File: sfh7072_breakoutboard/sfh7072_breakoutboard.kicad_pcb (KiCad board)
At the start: 2 copper layers, 24.5 x 25 mm, 11 parts, among them J1 C_01x06, J2 C_01x04

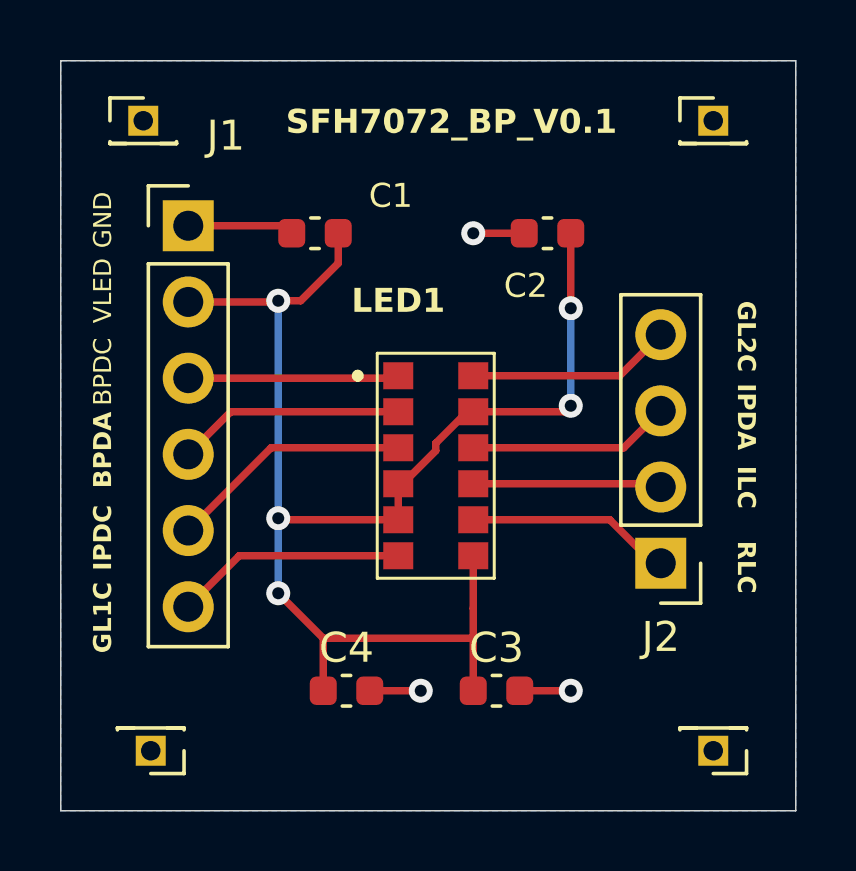
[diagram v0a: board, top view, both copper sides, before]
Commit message: sfh7072 board with separate anode for all leds
- separate anode and cathode connector for all leds
  and photodiodes

Signed-off-by: Mika Laitio <lamikr@gmail.com>
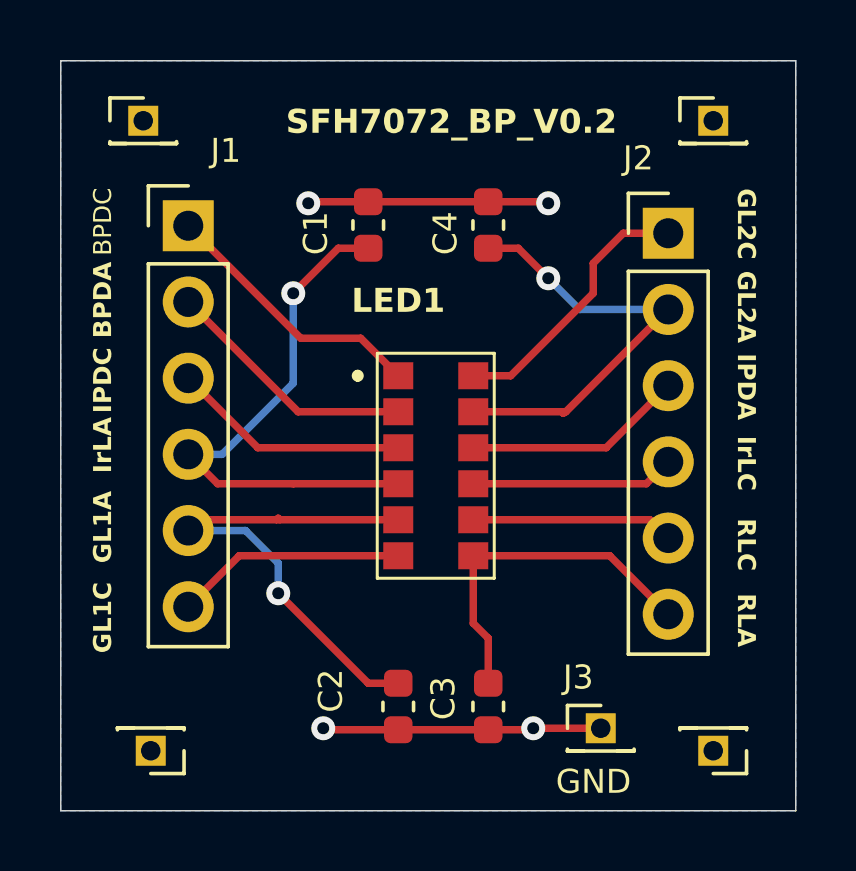
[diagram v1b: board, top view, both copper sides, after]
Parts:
- added J3: Conn_01x01_Pin, Connector_PinHeader_1.27mm:PinHeader_1x01_P1.27mm_Vertical, F.Cu at (37.8, 37.0)
- J2: value C_01x04 -> Conn_01x06_Pin; footprint Connector_PinHeader_2.54mm:PinHeader_1x04_P2.54mm_Vertical -> Connector_PinHeader_2.54mm:PinHeader_1x06_P2.54mm_Vertical
- moved C2 16.5 mm to (31.0, 36.3), turned to -90 degrees
- moved C4 16.2 mm to (34.0, 20.2), turned to 90 degrees
- moved J2 11.0 mm to (40.0, 20.5), turned to 0 degrees
- moved C1 1.80 mm to (30.0, 20.2), turned to 90 degrees
- moved C3 0.59 mm to (34.0, 36.3), turned to -90 degrees
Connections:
- C1 pad 1: EXT_LED_VSUPPLY -> EXT_IRDA_LED_A
- C2 pad 1: EXT_LED_VSUPPLY -> EXT_GR_LED1_A
- C3 pad 1: EXT_LED_VSUPPLY -> EXT_RED_LED_A
- C4 pad 1: EXT_LED_VSUPPLY -> EXT_GR_LED2_A
- J1 pad 1: GND -> EXT_BROADB_PD_C
- J1 pad 2: EXT_LED_VSUPPLY -> EXT_BROADB_PD_A
- J1 pad 3: EXT_BROADB_PD_C -> EXT_IRDA_PD_C
- J1 pad 4: EXT_BROADB_PD_A -> EXT_IRDA_LED_A
- J1 pad 5: EXT_IRDA_PD_C -> EXT_GR_LED1_A
- J2 pad 1: EXT_RED_LED_C -> EXT_GR_LED2_C
- J2 pad 2: EXT_IRDA_LED_C -> EXT_GR_LED2_A
- J2 pad 4: EXT_GR_LED2_C -> EXT_IRDA_LED_C
- LED1 pad 11: EXT_LED_VSUPPLY -> EXT_GR_LED2_A
- LED1 pad 4: EXT_LED_VSUPPLY -> EXT_IRDA_LED_A
- LED1 pad 5: EXT_LED_VSUPPLY -> EXT_GR_LED1_A
- LED1 pad 7: EXT_LED_VSUPPLY -> EXT_RED_LED_A
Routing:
- net EXT_LED_VSUPPLY: track 47.7 -> 0.00 mm, vias 5 -> 0
- net EXT_IRDA_LED_A: track 0.00 -> 18.0 mm, vias 0 -> 1
- net EXT_GR_LED1_A: track 0.00 -> 16.9 mm, vias 0 -> 1
- net EXT_GR_LED2_A: track 0.00 -> 14.8 mm, vias 0 -> 1
- net EXT_RED_LED_A: track 0.00 -> 11.8 mm
- net GND: track 8.65 -> 17.3 mm, vias 3 -> 4
- net EXT_GR_LED2_C: track 6.82 -> 9.05 mm
- net EXT_BROADB_PD_C: track 7.03 -> 9.07 mm
- net EXT_BROADB_PD_A: track 7.59 -> 8.52 mm
- net EXT_IRDA_PD_A: track 6.76 -> 7.36 mm
- net EXT_IRDA_LED_C: track 6.30 -> 6.80 mm
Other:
- board text added: "GL1A"
- board text added: "GL2A"
- board text added: "IrLA"
- board text added: "IrLC"
- board text added: "RLA"
- board text added: "SFH7072_BP_V0.2"
- board text removed: "ILC"
- board text removed: "SFH7072_BP_V0.1"
- board text removed: "VLED"
